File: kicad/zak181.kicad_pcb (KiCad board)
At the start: 4 copper layers, 215.3 x 96.8 mm, 123 parts, among them IC1 Z180, J1 JTAG, J10 DE15, J2 DB25_Receptacle_MountingHoles, J3 Compact Flash, J4 Speaker, J5 Keyboard, J7 DSUB-9, J8 USB C, J9 Reset, Q2 BC547, Q3 BC547, Q4 BC547, Q5 BC547, SW1 Reset, U17 LM386, U18 NE555P, U2 Z80 PIO A, U20 XC95108PC84, U21 74HC377, U22 74HC244, U23 27C64, U24 74HC166, U25 MAX232, U26 CH340N, U27 62256, U28 AS6C4008, U29 27C128, U3 AY-3-8912, U30 74HC377, U31 ZAK181MD (GAL16V8), U32 74HC157, U33 ZAK181AY (GAL16V8), U40 AS6C4008, U8 74HC138, X1 25.175 MHz, Y2 12.288 MHz

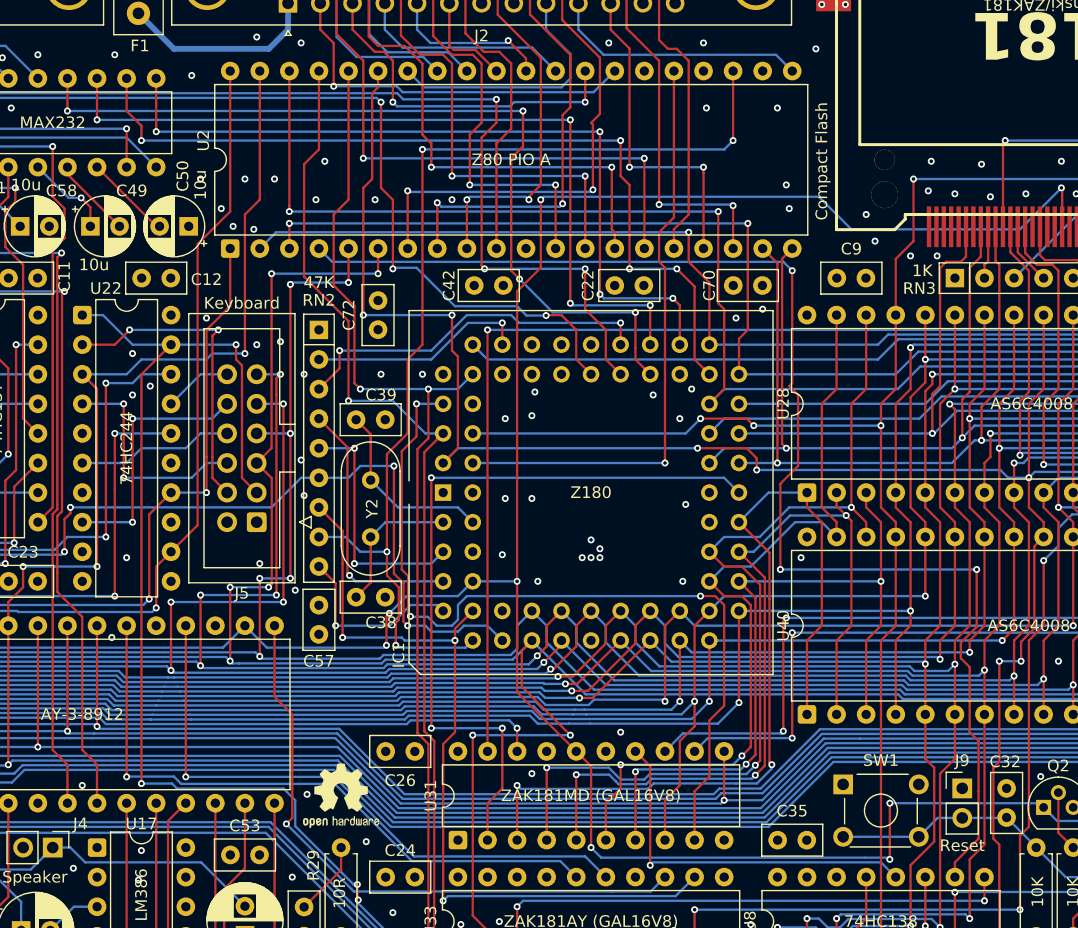
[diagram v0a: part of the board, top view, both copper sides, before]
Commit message: hw: rotate keyboard connector, move reset connector
- previous keyboard connector rotatation was indeed good already
- move reset connector to remove interference with the keyboard
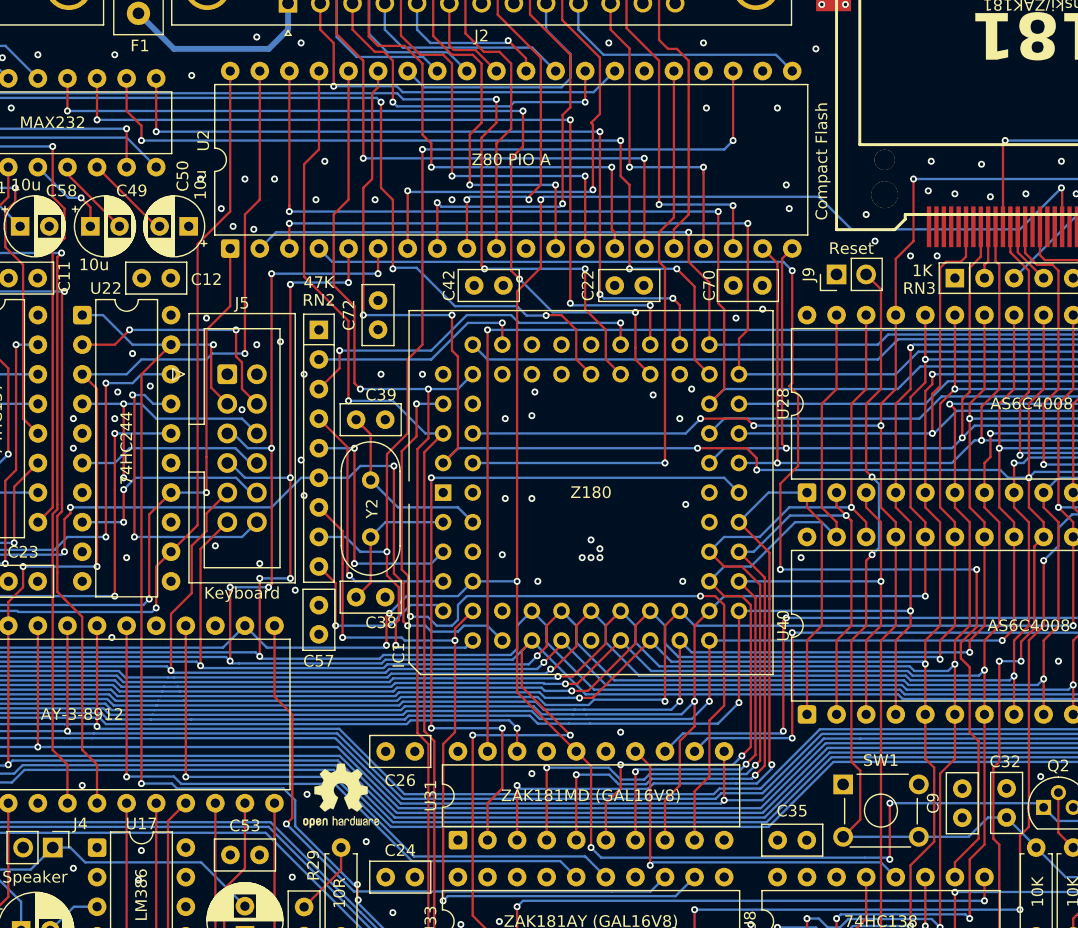
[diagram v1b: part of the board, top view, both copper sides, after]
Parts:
- moved C9 47.6 mm to (193.7, 124.4), turned to 90 degrees
- moved J9 45.4 mm to (182.9, 77.8), turned to 90 degrees
- moved J5 12.9 mm to (130.6, 86.4), turned to 0 degrees
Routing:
- net Net-(J9-Pin_2): track 25.8 -> 77.5 mm, vias 0 -> 2
- net Net-(J5-Pin_12): track 5.86 -> 26.9 mm, vias 0 -> 2
- net /A3: track 218.9 -> 198.5 mm, vias 6 -> 3
- net /A2: track 238.6 -> 221.1 mm, vias 7 -> 4
- net /cpu/~{KEYBOARD}: track 146.1 -> 136.5 mm
- net Net-(J5-Pin_4): track 26.9 -> 20.8 mm
- net /A0: track 297.9 -> 301.1 mm, vias 10 -> 11
- net Net-(J5-Pin_10): track 21.8 -> 18.7 mm
- net Net-(J5-Pin_6): track 19.3 -> 22.4 mm
- net /A1: track 261.4 -> 264.4 mm
- net Net-(J5-Pin_8): track 13.5 -> 16.0 mm
- net GND: vias 268 -> 273
